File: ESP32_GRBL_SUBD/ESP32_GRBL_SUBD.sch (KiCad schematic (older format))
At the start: 51 parts, among them J1 DB25_Female_MountingHoles, J10 Screw_Terminal_01x02, J11 Screw_Terminal_01x02, J12 Screw_Terminal_01x02, J13 Screw_Terminal_01x02, J2 Micro_SD_Card, J3 Conn_01x19_Female, J3a1 Conn_01x19_Female, J4 Conn_01x19_Female, J4a1 Conn_01x19_Female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

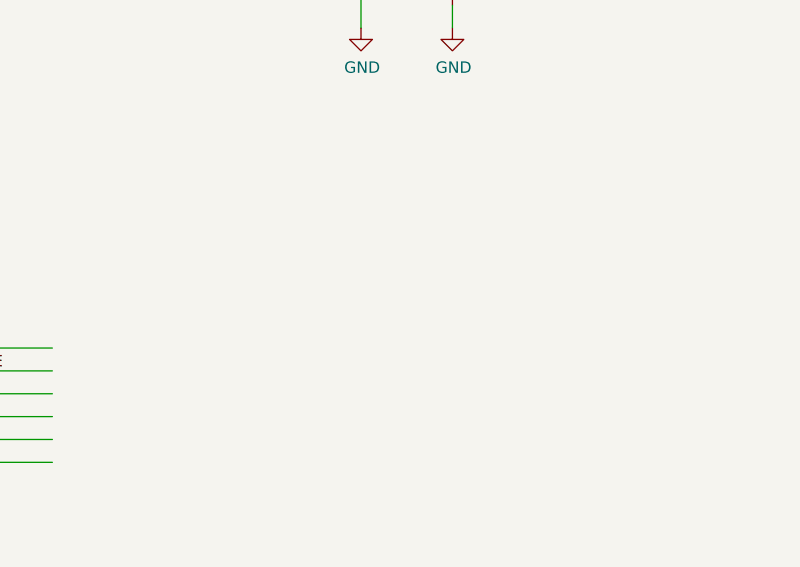
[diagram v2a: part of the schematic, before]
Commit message: added decoupling Cs
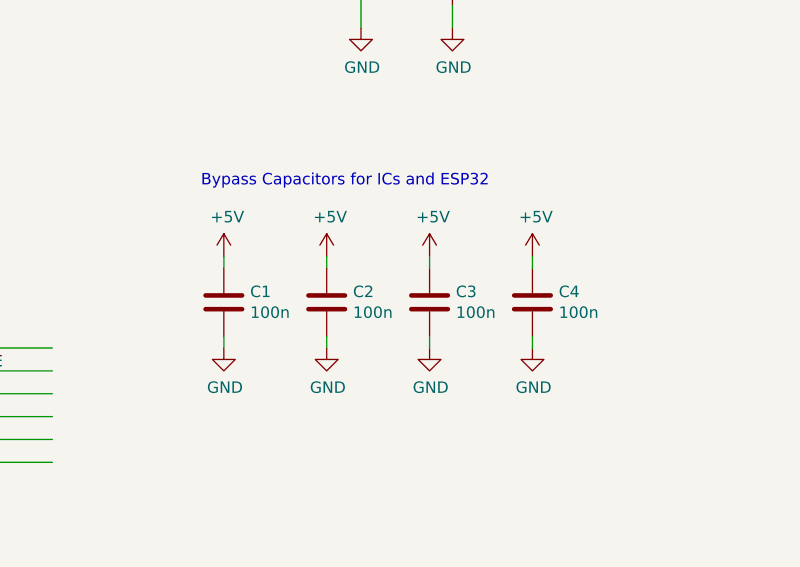
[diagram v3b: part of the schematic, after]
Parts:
- added C1, C2, C3, C4: 100n, Capacitor_SMD:C_0603_1608Metric, symbol Device:C
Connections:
- wire segments 306 -> 314
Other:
- note added: "Bypass Capacitors for ICs and ESP32"
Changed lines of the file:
@@
 Text Notes 11850 10150 0    79   ~ 16
 https://github.com/JochiSt/ESP32_GRBL_SUBD
+$Comp
+L Device:C C1
+U 1 1 5F61C3E6
+P 13650 5150
+F 0 "C1" H 13765 5196 50  0000 L CNN
+F 1 "100n" H 13765 5105 50  0000 L CNN
+F 2 "Capacitor_SMD:C_0603_1608Metric" H 13688 5000 50  0001 C CNN
+F 3 "~" H 13650 5150 50  0001 C CNN
+	1    13650 5150
+	1    0    0    -1
+$EndComp
+$Comp
+L Device:C C2
+U 1 1 5F61CBA2
+P 14100 5150
+F 0 "C2" H 14215 5196 50  0000 L CNN
+F 1 "100n" H 14215 5105 50  0000 L CNN
+F 2 "Capacitor_SMD:C_0603_1608Metric" H 14138 5000 50  0001 C CNN
+F 3 "~" H 14100 5150 50  0001 C CNN
+	1    14100 5150
+	1    0    0    -1
+$EndComp
+$Comp
+L Device:C C3
+U 1 1 5F63A437
+P 14550 5150
+F 0 "C3" H 14665 5196 50  0000 L CNN
+F 1 "100n" H 14665 5105 50  0000 L CNN
+F 2 "Capacitor_SMD:C_0603_1608Metric" H 14588 5000 50  0001 C CNN
+F 3 "~" H 14550 5150 50  0001 C CNN
+	1    14550 5150
+	1    0    0    -1
+$EndComp
+$Comp
+L Device:C C4
+U 1 1 5F657EDD
+P 15000 5150
+F 0 "C4" H 15115 5196 50  0000 L CNN
+F 1 "100n" H 15115 5105 50  0000 L CNN
+F 2 "Capacitor_SMD:C_0603_1608Metric" H 15038 5000 50  0001 C CNN
+F 3 "~" H 15000 5150 50  0001 C CNN
+	1    15000 5150
+	1    0    0    -1
+$EndComp
+$Comp
+L power:GND #PWR06
+U 1 1 5F67598B
+P 13650 5350
+F 0 "#PWR06" H 13650 5100 50  0001 C CNN
+F 1 "GND" H 13655 5177 50  0000 C CNN
+F 2 "" H 13650 5350 50  0001 C CNN
+F 3 "" H 13650 5350 50  0001 C CNN
+	1    13650 5350
+	1    0    0    -1
+$EndComp
+$Comp
+L power:GND #PWR08
+U 1 1 5F693348
+P 14100 5350
+F 0 "#PWR08" H 14100 5100 50  0001 C CNN
+F 1 "GND" H 14105 5177 50  0000 C CNN
+F 2 "" H 14100 5350 50  0001 C CNN
+F 3 "" H 14100 5350 50  0001 C CNN
+	1    14100 5350
+	1    0    0    -1
+$EndComp
+$Comp
+L power:GND #PWR021
+U 1 1 5F6B0C0B
+P 14550 5350
+F 0 "#PWR021" H 14550 5100 50  0001 C CNN
+F 1 "GND" H 14555 5177 50  0000 C CNN
+F 2 "" H 14550 5350 50  0001 C CNN
+F 3 "" H 14550 5350 50  0001 C CNN
+	1    14550 5350
+	1    0    0    -1
+$EndComp
+$Comp
+L power:GND #PWR045
+U 1 1 5F6CE501
+P 15000 5350
+F 0 "#PWR045" H 15000 5100 50  0001 C CNN
+F 1 "GND" H 15005 5177 50  0000 C CNN
+F 2 "" H 15000 5350 50  0001 C CNN
+F 3 "" H 15000 5350 50  0001 C CNN
+	1    15000 5350
+	1    0    0    -1
+$EndComp
+$Comp
+L power:+5V #PWR05
+U 1 1 5F6EBE95
+P 13650 4950
+F 0 "#PWR05" H 13650 4800 50  0001 C CNN
+F 1 "+5V" H 13665 5123 50  0000 C CNN
+F 2 "" H 13650 4950 50  0001 C CNN
+F 3 "" H 13650 4950 50  0001 C CNN
+	1    13650 4950
+	1    0    0    -1
+$EndComp
+$Comp
+L power:+5V #PWR07
+U 1 1 5F7097CB
+P 14100 4950
+F 0 "#PWR07" H 14100 4800 50  0001 C CNN
+F 1 "+5V" H 14115 5123 50  0000 C CNN
+F 2 "" H 14100 4950 50  0001 C CNN
+F 3 "" H 14100 4950 50  0001 C CNN
+	1    14100 4950
+	1    0    0    -1
+$EndComp
+$Comp
+L power:+5V #PWR020
+U 1 1 5F72709F
+P 14550 4950
+F 0 "#PWR020" H 14550 4800 50  0001 C CNN
+F 1 "+5V" H 14565 5123 50  0000 C CNN
+F 2 "" H 14550 4950 50  0001 C CNN
+F 3 "" H 14550 4950 50  0001 C CNN
+	1    14550 4950
+	1    0    0    -1
+$EndComp
+$Comp
+L power:+5V #PWR044
+U 1 1 5F7449AC
+P 15000 4950
+F 0 "#PWR044" H 15000 4800 50  0001 C CNN
+F 1 "+5V" H 15015 5123 50  0000 C CNN
+F 2 "" H 15000 4950 50  0001 C CNN
+F 3 "" H 15000 4950 50  0001 C CNN
+	1    15000 4950
+	1    0    0    -1
+$EndComp
+Wire Wire Line
+	15000 5300 15000 5350
+Wire Wire Line
+	15000 4950 15000 5000
+Wire Wire Line
+	14550 4950 14550 5000
+Wire Wire Line
+	14550 5300 14550 5350
+Wire Wire Line
+	14100 5350 14100 5300
+Wire Wire Line
+	14100 4950 14100 5000
+Wire Wire Line
+	13650 4950 13650 5000
+Wire Wire Line
+	13650 5300 13650 5350
+Text Notes 13550 4650 0    50   ~ 0
+Bypass Capacitors for ICs and ESP32
 $EndSCHEMATC

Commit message: some cleanup and connections of U0RX / TX and EN to second pin header
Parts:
- added C5: 1u, Capacitor_SMD:C_0603_1608Metric, symbol Device:C
- added C6, C7: 100n, Capacitor_SMD:C_0603_1608Metric, symbol Device:C
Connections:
- net labels added: EN, U0RX, U0TX
- wire segments 314 -> 326
- no-connect marks 18 -> 12
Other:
- moved on the sheet: D1, D2, D3, D4, D5, H1, H2, H3, H4, J10, J11, J12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

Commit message: added placement variant of first version
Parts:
- R23, R24, R25, R26, R27, R28, R30, R32: value 0R -> dnp
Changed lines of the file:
@@
 P 10100 3250
 F 0 "R30" H 10170 3296 50  0000 L CNN
-F 1 "0R" H 10170 3205 50  0000 L CNN
+F 1 "dnp" H 10170 3205 50  0000 L CNN
 F 2 "Resistor_SMD:R_0603_1608Metric" V 10030 3250 50  0001 C CNN
 F 3 "~" H 10100 3250 50  0001 C CNN
@@
 P 9250 3250
 F 0 "R27" H 9320 3296 50  0000 L CNN
-F 1 "0R" H 9320 3205 50  0000 L CNN
+F 1 "dnp" H 9320 3205 50  0000 L CNN
 F 2 "Resistor_SMD:R_0603_1608Metric" V 9180 3250 50  0001 C CNN
 F 3 "~" H 9250 3250 50  0001 C CNN
@@
 P 9000 3250
 F 0 "R26" H 9070 3296 50  0000 L CNN
-F 1 "0R" H 9070 3205 50  0000 L CNN
+F 1 "dnp" H 9070 3205 50  0000 L CNN
 F 2 "Resistor_SMD:R_0603_1608Metric" V 8930 3250 50  0001 C CNN
 F 3 "~" H 9000 3250 50  0001 C CNN
@@
 P 8350 3250
 F 0 "R24" H 8420 3296 50  0000 L CNN
-F 1 "0R" H 8420 3205 50  0000 L CNN
+F 1 "dnp" H 8420 3205 50  0000 L CNN
 F 2 "Resistor_SMD:R_0603_1608Metric" V 8280 3250 50  0001 C CNN
 F 3 "~" H 8350 3250 50  0001 C CNN
@@
 P 8100 3250
 F 0 "R23" H 8170 3296 50  0000 L CNN
-F 1 "0R" H 8170 3205 50  0000 L CNN
+F 1 "dnp" H 8170 3205 50  0000 L CNN
 F 2 "Resistor_SMD:R_0603_1608Metric" V 8030 3250 50  0001 C CNN
 F 3 "~" H 8100 3250 50  0001 C CNN
@@
 P 9600 3250
 F 0 "R28" H 9670 3296 50  0000 L CNN
-F 1 "0R" H 9670 3205 50  0000 L CNN
+F 1 "dnp" H 9670 3205 50  0000 L CNN
 F 2 "Resistor_SMD:R_0603_1608Metric" V 9530 3250 50  0001 C CNN
 F 3 "~" H 9600 3250 50  0001 C CNN
@@
 P 8750 3250
 F 0 "R25" H 8820 3296 50  0000 L CNN
-F 1 "0R" H 8820 3205 50  0000 L CNN
+F 1 "dnp" H 8820 3205 50  0000 L CNN
 F 2 "Resistor_SMD:R_0603_1608Metric" V 8680 3250 50  0001 C CNN
 F 3 "~" H 8750 3250 50  0001 C CNN
@@
 P 9850 5550
 F 0 "R32" V 10057 5550 50  0000 C CNN
-F 1 "0R" V 9966 5550 50  0000 C CNN
+F 1 "dnp" V 9966 5550 50  0000 C CNN
 F 2 "Resistor_SMD:R_0603_1608Metric" V 9780 5550 50  0001 C CNN
 F 3 "~" H 9850 5550 50  0001 C CNN
